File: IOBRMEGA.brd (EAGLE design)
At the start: 86.4 x 53.3 mm, 21 parts, among them J1 Digital_0_7, J10 Power, J2 Analog, J3 Digital_8_13, J4 Analog, J5 Digital_0_7, J6 Digital_22_36, J7 Digital_23_37, J8 Digital_38_52, J9 Digital_39_53

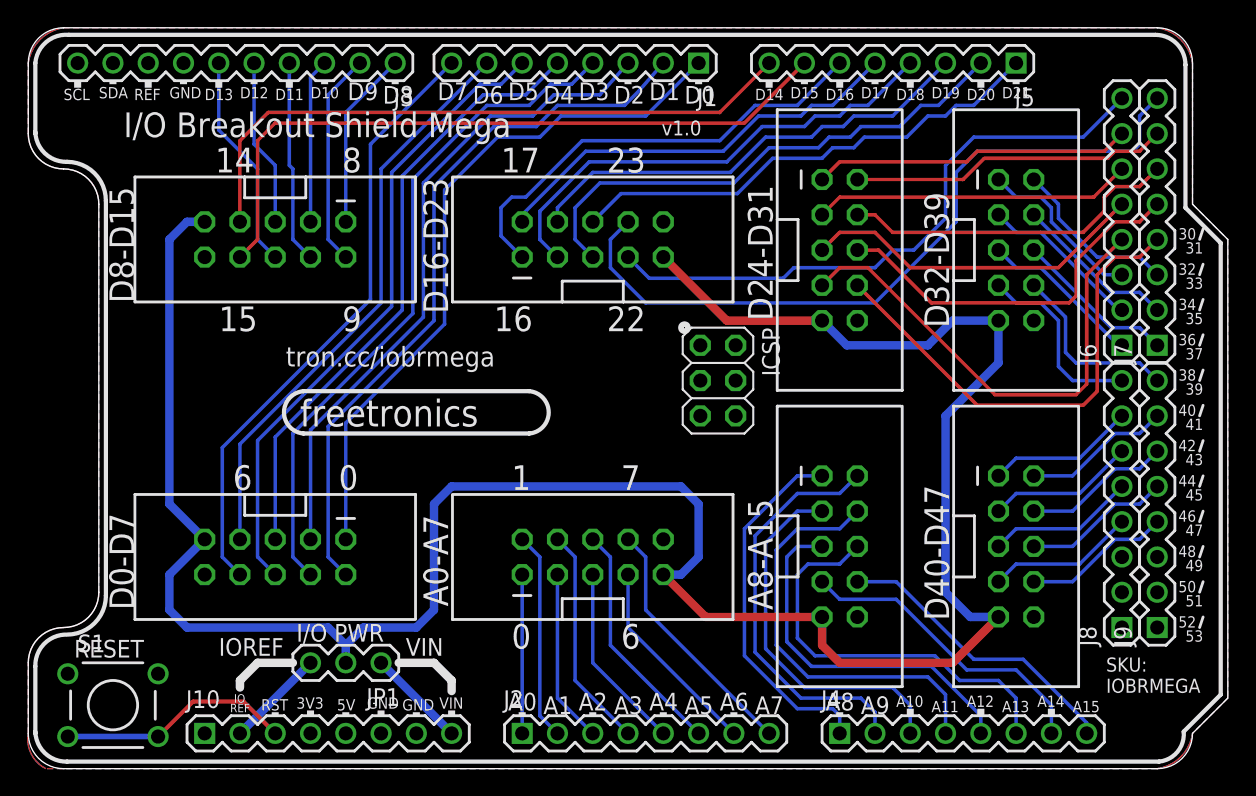
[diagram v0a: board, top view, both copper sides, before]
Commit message: Expanded headers to 2x6 to include IOREF and RESET for v2.0 release
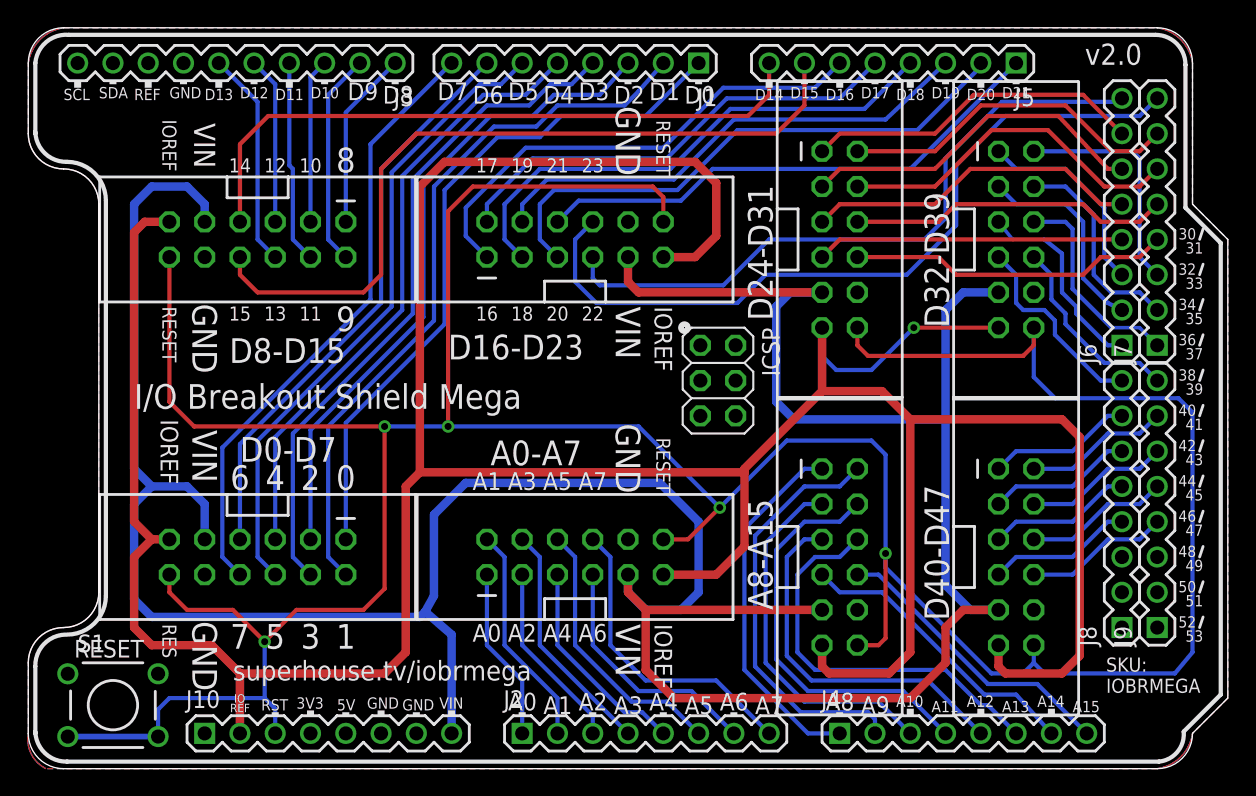
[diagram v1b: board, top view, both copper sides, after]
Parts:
- removed JP1: (no value), freetronics-master-v1.1:1X03
- J2: value Analog -> Analog_0_7
- J4: value Analog -> Analog_8_15
- J5: value Digital_0_7 -> Digital_14_21
- JP11, JP12, JP13, JP14, JP15, JP2, JP3, JP4: value M05X2SHD -> M06X2; device freetronics-original:2X5-SHROUDED -> freetronics-jon:2X6-SHROUDED
- S1: value (none) -> RESET
- moved JP14 7.73 mm to (33.0, 36.8)
- moved JP11 7.73 mm to (33.0, 14.0)
- moved JP3 7.22 mm to (69.8, 44.5)
- moved JP4 7.22 mm to (57.1, 44.5)
- moved JP2 5.73 mm to (69.8, 21.6)
- moved JP12 5.73 mm to (57.1, 21.6)
- moved JP13 5.24 mm to (22.9, 16.5)
- moved JP15 5.24 mm to (22.9, 39.4)
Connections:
- removed net IOVCC: JP1.2, JP11.9, JP12.9, JP13.9, JP14.9, JP15.9, JP2.9, JP3.9, JP4.9
- net IOREF: now also JP11.11, JP12.11, JP13.11, JP14.11, JP15.11, JP2.11, JP3.11, JP4.11; no longer JP1.3
- net RESET: now also JP11.12, JP12.12, JP13.12, JP14.12, JP15.12, JP2.12, JP3.12, JP4.12
- net VIN: now also JP11.9, JP12.9, JP13.9, JP14.9, JP15.9, JP2.9, JP3.9, JP4.9; no longer JP1.1
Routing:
- net IOREF: track 7.18 -> 258.2 mm, vias 0 -> 1
- net RESET: track 16.9 -> 254.8 mm, vias 0 -> 5
- net VIN: track 7.18 -> 234.3 mm
- net IOVCC: track 171.4 -> 0.00 mm
- net D30: track 35.1 -> 22.1 mm
- net D31: track 35.0 -> 23.2 mm
- net D15: track 50.6 -> 55.5 mm
- net D29: track 27.6 -> 23.2 mm
- net D33: track 12.3 -> 16.7 mm
- net D22: track 43.8 -> 47.9 mm
- net A7: track 18.2 -> 22.2 mm
- net D37: track 11.7 -> 15.1 mm
- net D35: track 11.7 -> 15.1 mm
- net A6: track 14.6 -> 17.9 mm
- net D34: track 11.7 -> 14.9 mm
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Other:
- board text added: "(C) 2017 SuperHouse Automation Pty Ltd Released under the TAPR Open Hardware License www.tapr.org/OHL"
- board text added: "G"
- board text added: "RES"
- board text added: "superhouse.tv/iobrmega"
- board text added: "v2.0"
- board text removed: "(C) 2014 Freetronics Pty Ltd Released under the TAPR Open Hardware License www.tapr.org/OHL"
- board text removed: "I/O PWR"
- board text removed: "VCC"
- board text removed: "freetronics"
- board text removed: "tron.cc/iobrmega"
- board text removed: "v1.0"

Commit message: Part swap to SuperHouse library to add 3D models
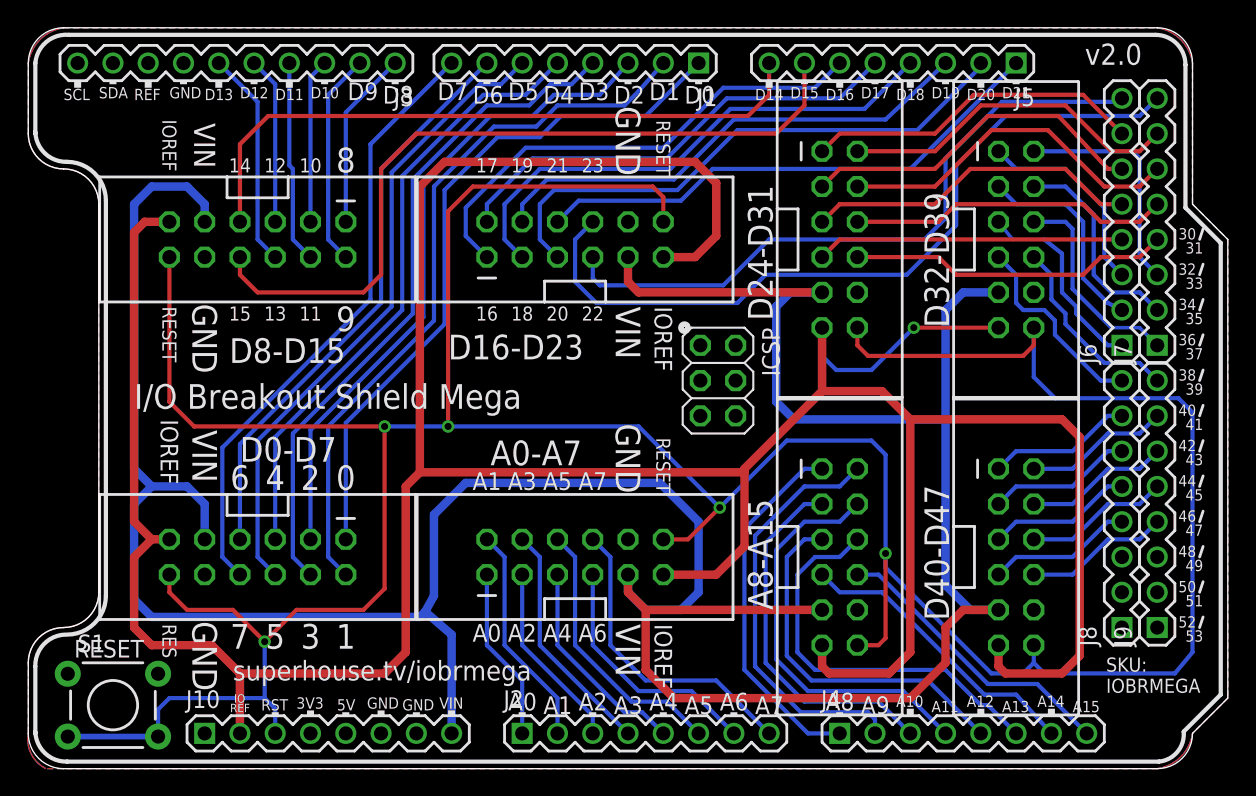
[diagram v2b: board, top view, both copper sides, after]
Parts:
- JP11, JP12, JP13, JP14, JP15, JP2, JP3, JP4: value M06X2 -> M06X2-SHROUDED; device freetronics-jon:2X6-SHROUDED -> SuperHouse-Connectors:2X6-SHROUDED
- S1: device freetronics-master-v1:TACTILE-PTH -> SuperHouse-Switches:TACTILE-PTH-6MM

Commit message: Updated for v2.1 release
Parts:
- J1, J5, J6, J7, J8, J9: device freetronics:1X08 -> SuperHouse-Connectors:1X08-P-BELOW
- J10, J2, J4: device freetronics-master-v1:1X08 -> SuperHouse-Connectors:1X08-P-BELOW
- J3: device freetronics-original:1X10 -> SuperHouse-Connectors:1X10-P-BELOW
- renumbered ICSP to J19, JP11 to J11, JP12 to J12, JP13 to J17, JP14 to J16, JP15 to J18, JP2 to J13, JP3 to J14, JP4 to J15
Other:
- board text added: "(C)2017-2019 SuperHouse Automation Pty Ltd Released under the TAPR Open Hardware License www.tapr.org/OHL"
- board text added: "by Jon Oxer"
- board text added: "v2.1"
- board text removed: "(C) 2017 SuperHouse Automation Pty Ltd Released under the TAPR Open Hardware License www.tapr.org/OHL"
- board text removed: "v2.0"

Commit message: Final tweaks for v2.1 release
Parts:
- J11, J12, J13, J14, J15, J16, J17, J18: value M06X2-SHROUDED -> M02X6-SHROUDED; device SuperHouse-Connectors:2X6-SHROUDED -> SuperHouse-Connectors:2X06-SHROUDED
